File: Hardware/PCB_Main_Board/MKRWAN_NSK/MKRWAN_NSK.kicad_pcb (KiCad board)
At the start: 2 copper layers, 86.3 x 97.5 mm, 29 parts, among them J1 Conn_01x05, J10 O2_Sensor, J13 Pont_diviseur, J2 TH_Deep_Sensor, J3 Other_Gaz_Sensor, J4 UV_IR_Sensor, J6 RGB_Sensor, J7 CO2_Sensor, J8 Pressure_Sensor, J9 TH_Surface_Sensor, U1 ARDUINO_MKR_WAN_1310

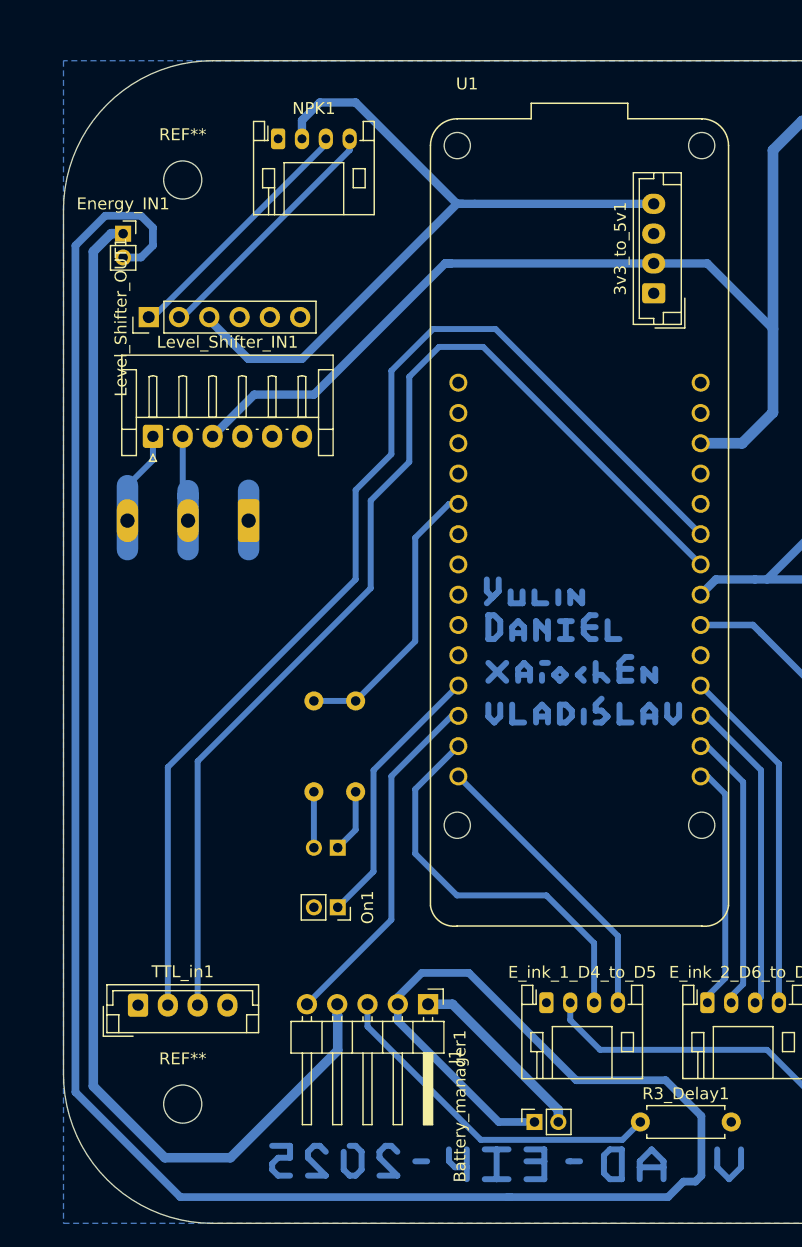
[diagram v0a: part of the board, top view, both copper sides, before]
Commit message: Hardware PCB - PCB v5 TTL fixed + Holes Alignment
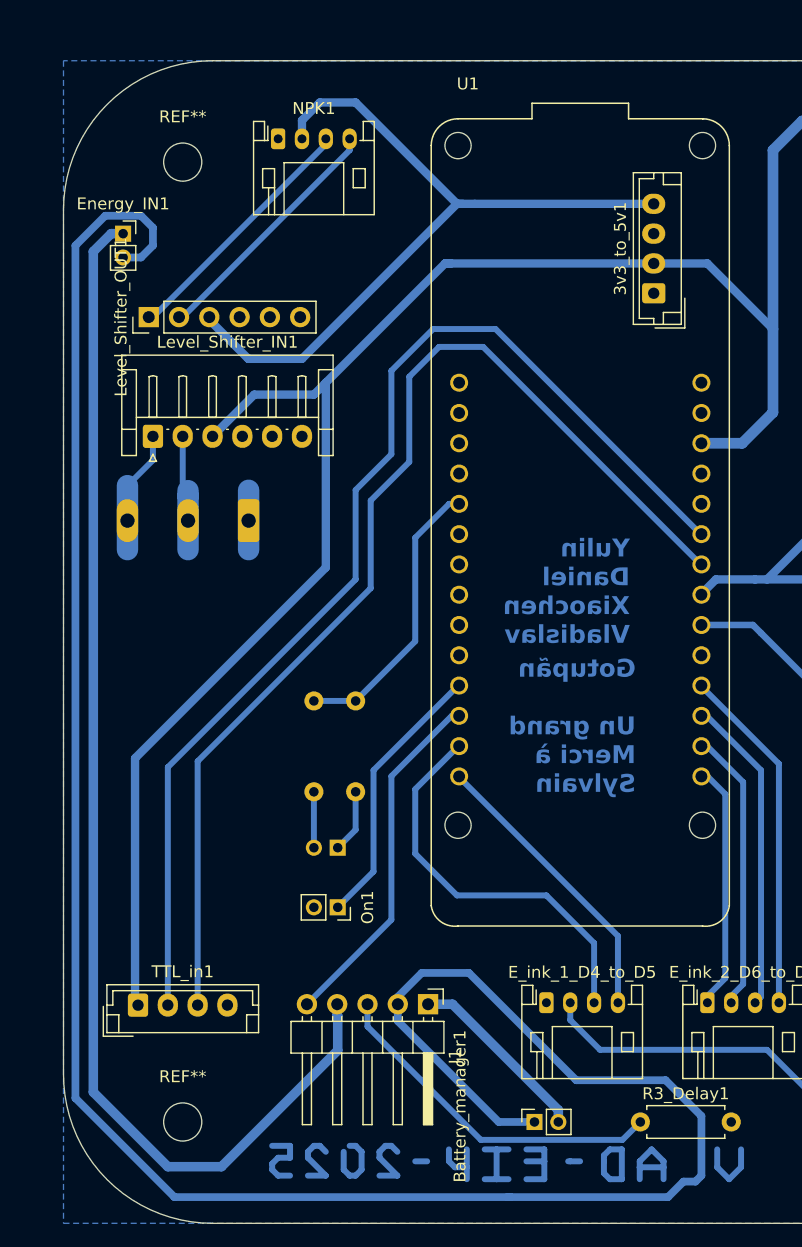
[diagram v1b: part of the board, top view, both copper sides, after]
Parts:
- moved REF** 1.50 mm to (186.5, 71.5)
- moved REF** 1.50 mm to (186.5, 152.0)
- moved U1 0.06 mm to (219.8, 101.7)
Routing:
- net /GND: track 107.3 -> 15.0 mm
- net /3v3: track 239.0 -> 297.9 mm
- net /3v3_bis: track 103.7 -> 104.6 mm
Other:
- board text added: "Gotupãn Un grand Merci à Sylvain"
- board text added: "Yulin Daniel Xiaochen Vladislav"
